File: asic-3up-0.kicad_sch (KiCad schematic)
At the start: 64 parts, among them J18 Conn_01x01, J3 Conn_01x01, J4 Conn_01x01, U28 MCP1824T-1202E/OT, U29 MCP1824T-1202E/OT, U30 MCP1824T-1202E/OT, U32 MCP1824T-0802E, U42 MCP1824T-0802E, U43 MCP1824T-0802E, U45 BM1362AC_MODE1, U46 BM1362AC_MODE0, U47 BM1362AC_MODE1

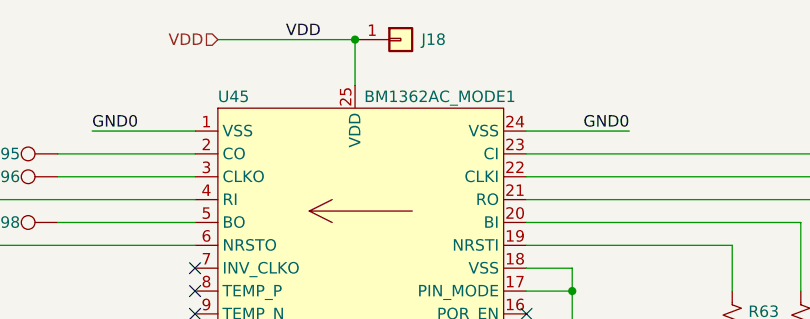
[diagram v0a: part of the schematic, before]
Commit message: remove all power pads, replace with planes, including on back layer. regenerate BOM
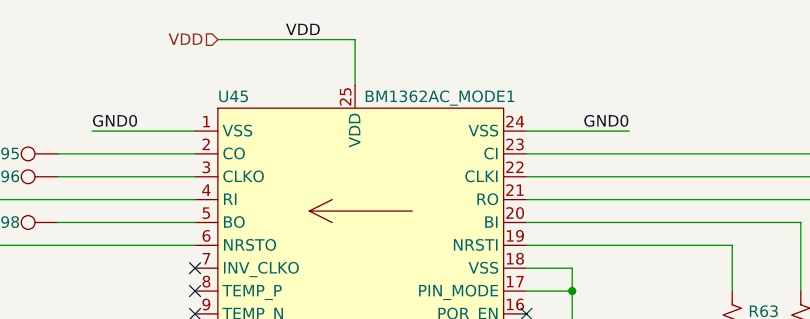
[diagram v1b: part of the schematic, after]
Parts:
- removed J18: Conn_01x01, emberone:14x9_powertab_L, symbol Connector_Generic:Conn_01x01
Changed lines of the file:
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@@
 	)
 	(junction
-		(at 248.92 54.61)
-		(diameter 0)
-		(color 0 0 0 0)
-	)
-	(junction
 		(at 271.78 199.39)
 		(diameter 0)
@@
 					(unit 1)
 				)
-			)
-		)
-	)
-	(symbol
-		(lib_id "Connector_Generic:Conn_01x01")
-		(at 254 54.61 0)
-		(unit 1)
-		(exclude_from_sim no)
-		(in_bom yes)
-		(on_board yes)
-		(dnp no)
-		(property "Reference" "J18"
-			(at 256.286 54.61 0)
-			(effects
-				(font
-					(size 1.27 1.27)
-				)
-				(justify left)
-			)
-		)
-		(property "Value" "Conn_01x01"
-			(at 256.54 55.8799 0)
-			(effects
-				(font
-					(size 1.27 1.27)
-				)
-				(justify left)
-				(hide yes)
-			)
-		)
-		(property "Footprint" "emberone:14x9_powertab_L"
-			(at 254 54.61 0)
-			(effects
-				(font
-					(size 1.27 1.27)
-				)
-				(hide yes)
-			)
-		)
-		(property "Datasheet" "~"
-			(at 254 54.61 0)
-			(effects
-				(font
-					(size 1.27 1.27)
-				)
-				(hide yes)
-			)
-		)
-		(property "Description" "powertab"
-			(at 254 54.61 0)
-			(effects
-				(font
-					(size 1.27 1.27)
-				)
-				(hide yes)
-			)
-		)
-		(pin "1"
-		)
-		(instances
-			(project "emberone"
-				(path "/b036224c-4cdf-48cc-81df-19bc5283ebd2/dea5684e-9ec9-4967-b9ef-d4ee852a3fa0"
-					(reference "J18")
-					(unit 1)
-				)
